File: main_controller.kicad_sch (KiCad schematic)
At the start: 1 part, among them U2 RP2040

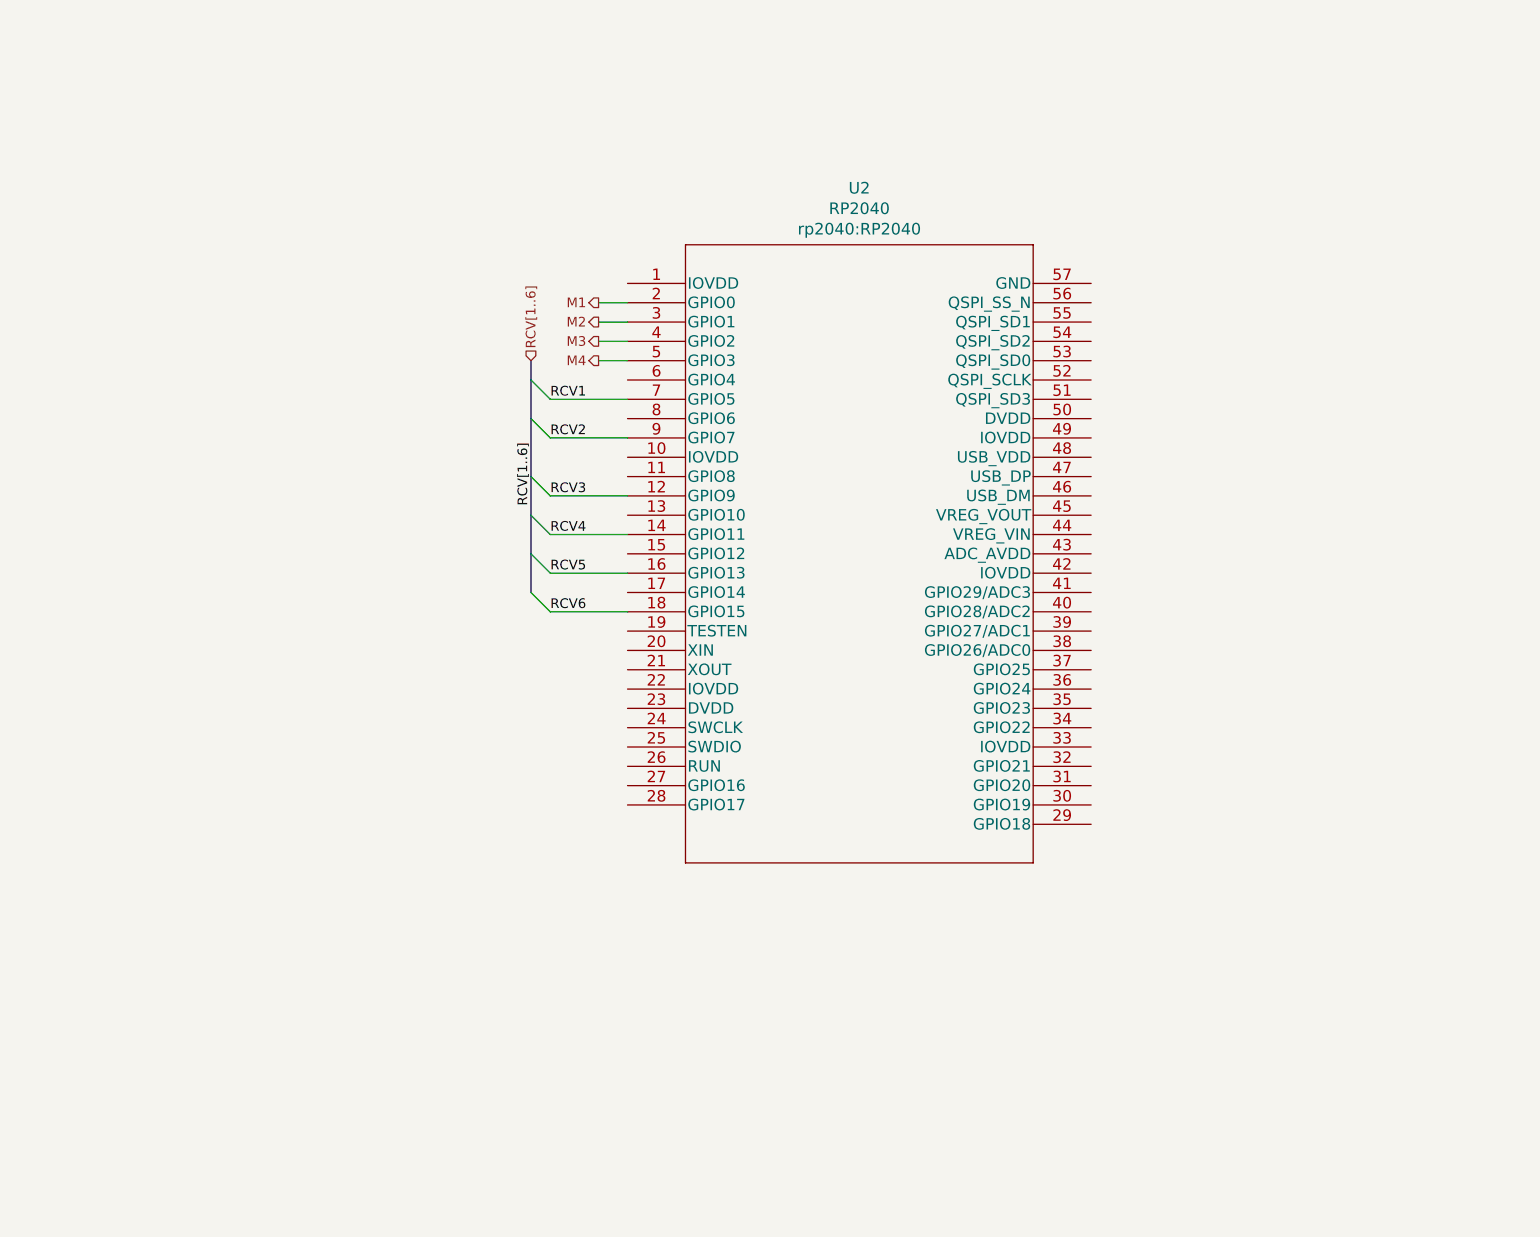
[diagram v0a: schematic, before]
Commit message: Initial schematic version
This is now a clean and ready version of the schematic:
That means:
- Schematic has been reviewed,
- It's fully annotated,
- All elements have been checked for availability with JLCPCB,
- Footprints were assigned,
- ERC is green.

No design changes should be added for this version until
the PCB is present and version is released.
Only bugfixes are possible now.
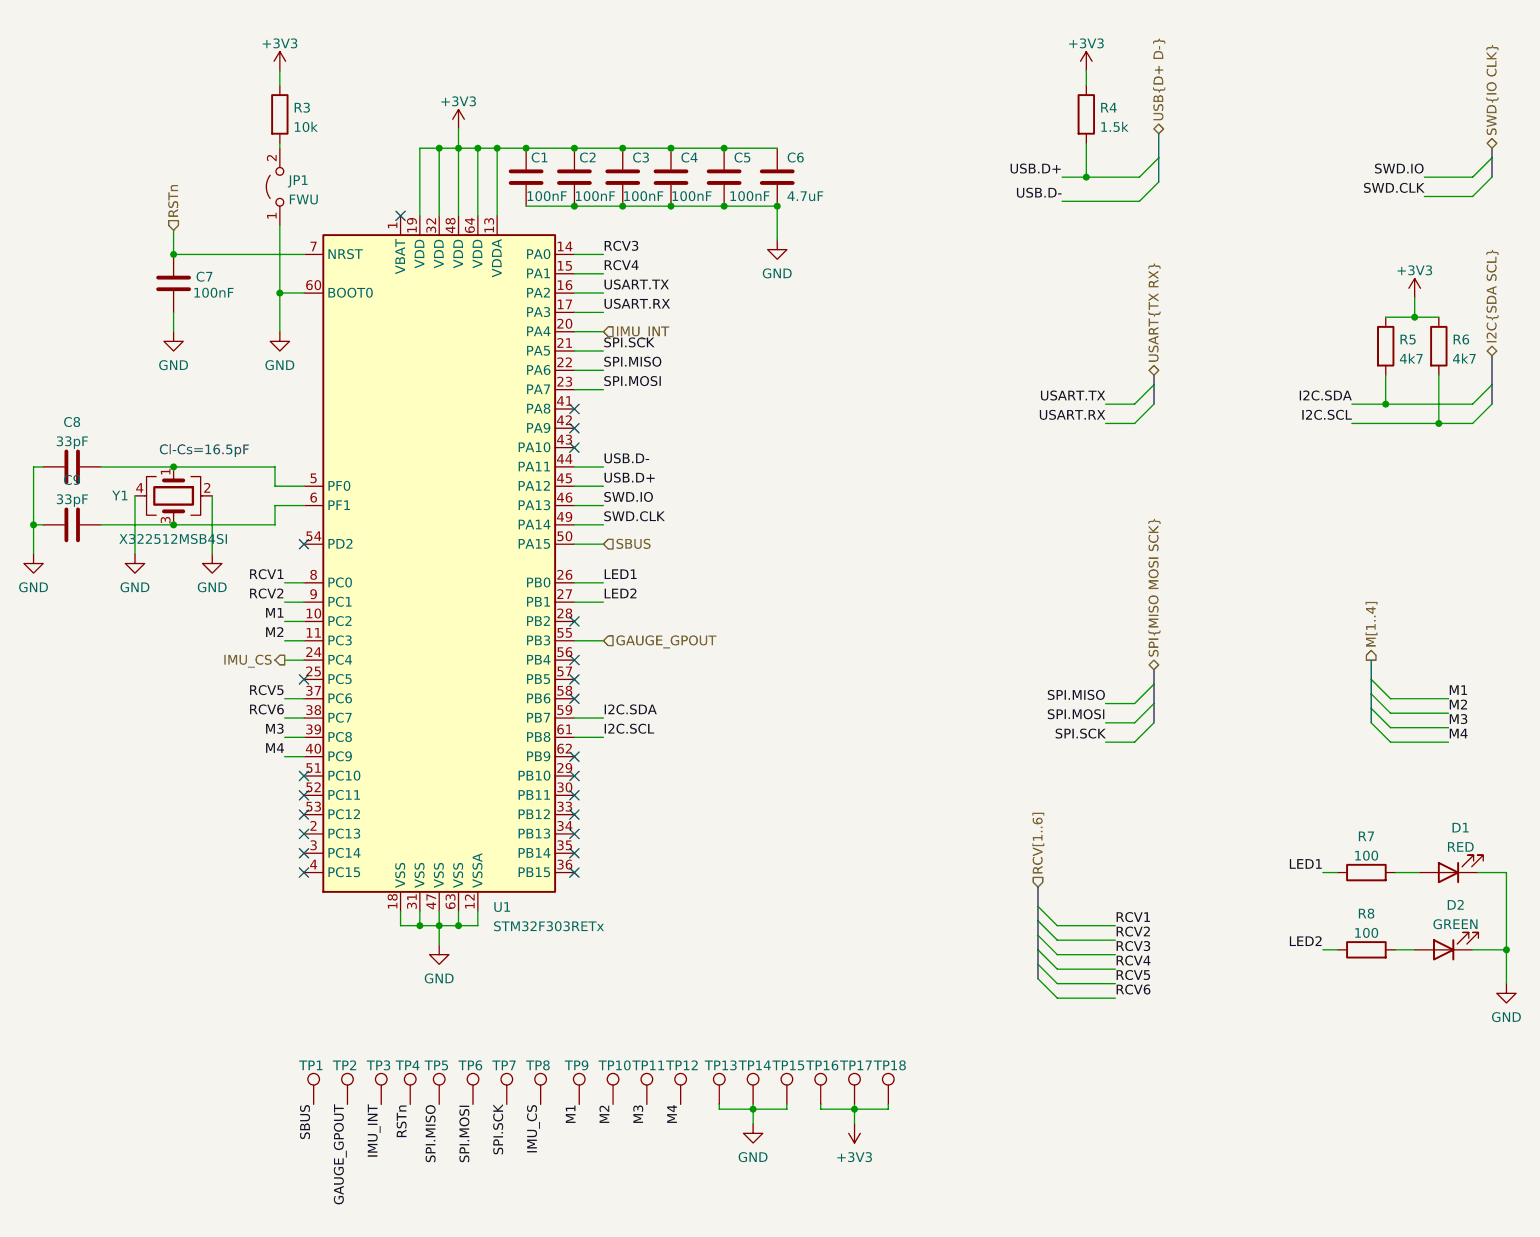
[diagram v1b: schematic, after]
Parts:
- removed U2: RP2040, rp2040:RP2040, symbol flight_controller_v2-rescue:RP2040-rp2040
- added C1, C2, C3, C4, C5, C7: 100nF, Capacitor_SMD:C_0402_1005Metric, symbol Device:C
- added C6: 4.7uF, Capacitor_SMD:C_0603_1608Metric, symbol Device:C
- added C8, C9: 33pF, Capacitor_SMD:C_0402_1005Metric, symbol Device:C
- added D1: RED, LED_SMD:LED_0402_1005Metric, symbol Device:LED
- added D2: GREEN, LED_SMD:LED_0402_1005Metric, symbol Device:LED
- added JP1: FWU, Connector_PinHeader_2.54mm:PinHeader_1x02_P2.54mm_Vertical, symbol Jumper:Jumper_2_Open
- added R3: 10k, Resistor_SMD:R_0402_1005Metric, symbol Device:R
- added R4: 1.5k, Resistor_SMD:R_0402_1005Metric, symbol Device:R
- added R5, R6: 4k7, Resistor_SMD:R_0402_1005Metric, symbol Device:R
- added R7, R8: 100, Resistor_SMD:R_0402_1005Metric, symbol Device:R
- added TP1, TP10, TP11, TP12, TP13, TP14, TP15, TP16, TP17, TP18, TP2, TP3, TP4, TP5, TP6, TP7, TP8, TP9: TestPoint, TestPoint:TestPoint_Pad_D1.0mm, symbol Connector:TestPoint
- added U1: STM32F303RETx, Package_QFP:LQFP-64_10x10mm_P0.5mm, symbol MCU_ST_STM32F3:STM32F303RETx
- added Y1: X322512MSB4SI, Crystal:Crystal_SMD_3225-4Pin_3.2x2.5mm, symbol Device:Crystal_GND24
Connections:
- net M1: now also TP9.1, U1.10 (PC2)
- net M2: now also TP10.1, U1.11 (PC3)
- net M3: now also TP11.1, U1.39 (PC8)
- net M4: now also TP12.1, U1.40 (PC9)
- net RCV1: now also U1.8 (PC0)
- net RCV2: now also U1.9 (PC1)
- net RCV3: now also U1.14 (PA0)
- net RCV4: now also U1.15 (PA1)
- net RCV5: now also U1.37 (PC6)
- net RCV6: now also U1.38 (PC7)
- new net: C8.2, U1.5 (PF0), Y1.1
- new net: C9.2, U1.6 (PF1), Y1.3
- new net: JP1.2 (B), R3.2
- new net: D1.2 (A), R7.2
- new net: D2.2 (A), R8.2
- new net +3V3: C1.1, C2.1, C3.1, C4.1, C5.1, C6.1, R3.1, R4.1, R5.1, R6.1, TP16.1, TP17.1, TP18.1, U1.13 (VDDA), U1.19 (VDD), U1.32 (VDD), U1.48 (VDD), U1.64 (VDD)
- new net GAUGE_GPOUT: TP2.1, U1.55 (PB3)
- new net GND: C1.2, C2.2, C3.2, C4.2, C5.2, C6.2, C7.2, C8.1, C9.1, D1.1 (K), D2.1 (K), JP1.1 (A), TP13.1, TP14.1, TP15.1, U1.12 (VSSA), U1.18 (VSS), U1.31 (VSS), U1.47 (VSS), U1.60 (BOOT0), U1.63 (VSS), Y1.2, Y1.4
- new net I2C.SCL: R6.2, U1.61 (PB8)
- new net I2C.SDA: R5.2, U1.59 (PB7)
- new net IMU_CS: TP8.1, U1.24 (PC4)
- new net IMU_INT: TP3.1, U1.20 (PA4)
- new net LED1: R7.1, U1.26 (PB0)
- new net LED2: R8.1, U1.27 (PB1)
- new net RSTn: C7.1, TP4.1, U1.7 (NRST)
- new net SBUS: TP1.1, U1.50 (PA15)
- new net SPI.MISO: TP5.1, U1.22 (PA6)
- new net SPI.MOSI: TP6.1, U1.23 (PA7)
- new net SPI.SCK: TP7.1, U1.21 (PA5)
- new net SWD.CLK: U1.49 (PA14)
- new net SWD.IO: U1.46 (PA13)
- new net USART.RX: U1.17 (PA3)
- new net USART.TX: U1.16 (PA2)
- new net USB.D+: R4.2, U1.45 (PA12)
- new net USB.D-: U1.44 (PA11)
- no-connect marks 0 -> 23
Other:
- note added: "Cl-Cs=16.5pF"

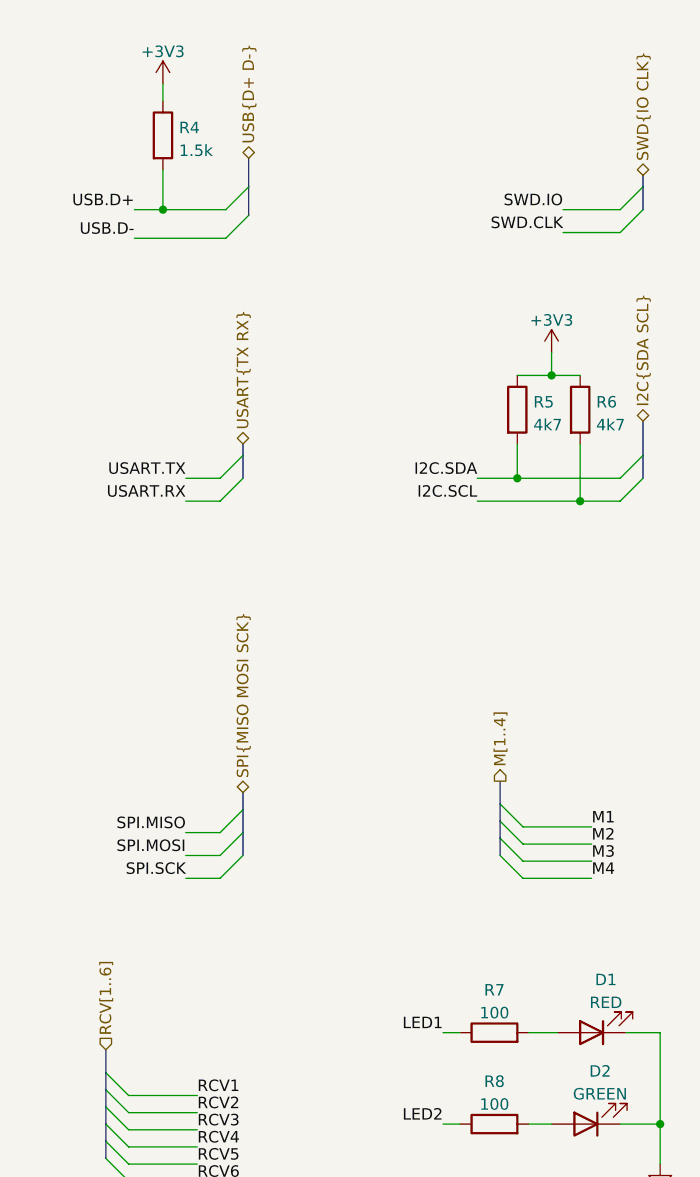
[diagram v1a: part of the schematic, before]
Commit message: Update footprints and add JLCPCB fields
Update some footprints which will suit better building the pcb
with JLCBPCB. Add fields to components sourced from JLCPCB
to be able to generate BOM.
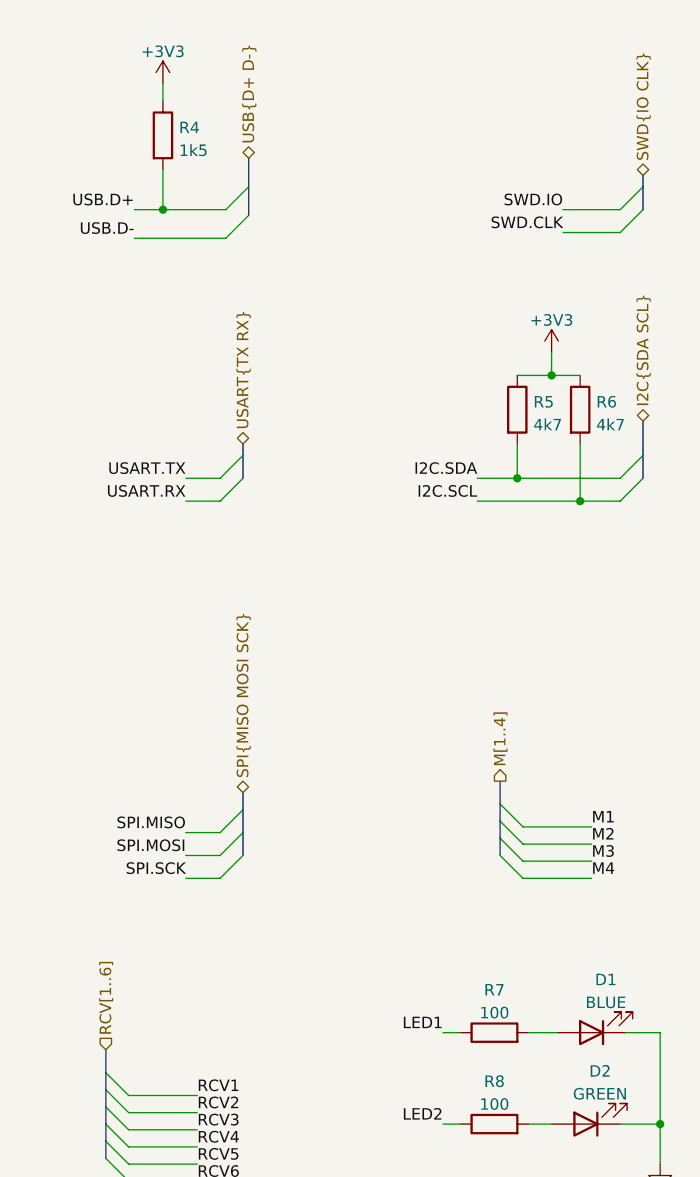
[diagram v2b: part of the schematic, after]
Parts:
- C1, C2, C3, C4, C5, C7: JLC (none) -> 0402; LCSC (none) -> C1525
- C6: footprint Capacitor_SMD:C_0603_1608Metric -> Capacitor_SMD:C_0402_1005Metric; JLC (none) -> 0402; LCSC (none) -> C23733
- C8, C9: JLC (none) -> 0402; LCSC (none) -> C1562
- D1: value RED -> BLUE; footprint LED_SMD:LED_0402_1005Metric -> LED_SMD:LED_0603_1608Metric; JLC (none) -> 0603; LCSC (none) -> C72041
- D2: footprint LED_SMD:LED_0402_1005Metric -> LED_SMD:LED_0603_1608Metric; JLC (none) -> 0603; LCSC (none) -> C72043
- R3: JLC (none) -> 0402; LCSC (none) -> C25744
- R4: value 1.5k -> 1k5; JLC (none) -> 0402; LCSC (none) -> C25867
- R5, R6: JLC (none) -> 0402; LCSC (none) -> C25900
- R7, R8: JLC (none) -> 0402; LCSC (none) -> C25076
- U1: JLC (none) -> LQFP-64(10x10); LCSC (none) -> C183214
- Y1: JLC (none) -> SMD3225-4P; LCSC (none) -> C9002
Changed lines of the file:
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@@
+      (effects (font (size 1.27 1.27)) hide)
+    )
+    (property "JLC" "LQFP-64(10x10)" (id 4) (at 89.535 96.52 0)
+      (effects (font (size 1.27 1.27)) hide)
+    )
+    (property "LCSC" "C183214" (id 5) (at 89.535 96.52 0)
       (effects (font (size 1.27 1.27)) hide)
     )
@@
       (effects (font (size 1.27 1.27)) (justify left))
     )
-    (property "Value" "1.5k" (id 1) (at 176.403 39.1672 0)
+    (property "Value" "1k5" (id 1) (at 176.403 39.1672 0)
       (effects (font (size 1.27 1.27)) (justify left))
     )
@@
     )
     (property "Datasheet" "~" (id 3) (at 174.625 37.465 0)
+      (effects (font (size 1.27 1.27)) hide)
+    )
+    (property "JLC" "0402" (id 4) (at 174.625 37.465 0)
+      (effects (font (size 1.27 1.27)) hide)
+    )
+    (property "LCSC" " C25867" (id 5) (at 174.625 37.465 0)
       (effects (font (size 1.27 1.27)) hide)
     )
@@
     )
     (property "Datasheet" "~" (id 3) (at 213.995 67.945 0)
+      (effects (font (size 1.27 1.27)) hide)
+    )
+    (property "JLC" "0402" (id 4) (at 213.995 67.945 0)
+      (effects (font (size 1.27 1.27)) hide)
+    )
+    (property "LCSC" " C25900" (id 5) (at 213.995 67.945 0)
       (effects (font (size 1.27 1.27)) hide)
     )
@@
       (effects (font (size 1.27 1.27)) hide)
     )
+    (property "JLC" "0402" (id 4) (at 211.455 137.16 0)
+      (effects (font (size 1.27 1.27)) hide)
+    )
+    (property "LCSC" " C25076" (id 5) (at 211.455 137.16 0)
+      (effects (font (size 1.27 1.27)) hide)
+    )
     (pin "1")
     (pin "2")
@@
     )
     (property "Datasheet" "~" (id 3) (at 68.58 37.465 0)
+      (effects (font (size 1.27 1.27)) hide)
+    )
+    (property "JLC" "0402" (id 4) (at 68.58 37.465 0)
+      (effects (font (size 1.27 1.27)) hide)
+    )
+    (property "LCSC" " C25744" (id 5) (at 68.58 37.465 0)
       (effects (font (size 1.27 1.27)) hide)
     )
@@
       (effects (font (size 1.27 1.27)) hide)
     )
+    (property "JLC" "0402" (id 4) (at 41.275 83.82 0)
+      (effects (font (size 1.27 1.27)) hide)
+    )
+    (property "LCSC" "C1562" (id 5) (at 41.275 83.82 0)
+      (effects (font (size 1.27 1.27)) hide)
+    )
     (pin "1")
     (pin "2")
@@
       (effects (font (size 1.27 1.27)) hide)
     )
+    (property "JLC" "0402" (id 4) (at 127 45.72 0)
+      (effects (font (size 1.27 1.27)) hide)
+    )
+    (property "LCSC" "C1525" (id 5) (at 127 45.72 0)
+      (effects (font (size 1.27 1.27)) hide)
+    )
     (pin "1")
     (pin "2")
@@
       (effects (font (size 1.27 1.27)) hide)
     )
+    (property "JLC" "0402" (id 4) (at 120.015 45.72 0)
+      (effects (font (size 1.27 1.27)) hide)
+    )
+    (property "LCSC" "C1525" (id 5) (at 120.015 45.72 0)
+      (effects (font (size 1.27 1.27)) hide)
+    )
     (pin "1")
     (pin "2")
@@
     )
     (property "Datasheet" "~" (id 3) (at 100.965 45.72 0)
+      (effects (font (size 1.27 1.27)) hide)
+    )
+    (property "JLC" "0402" (id 4) (at 100.965 45.72 0)
+      (effects (font (size 1.27 1.27)) hide)
+    )
+    (property "LCSC" "C1525" (id 5) (at 100.965 45.72 0)
       (effects (font (size 1.27 1.27)) hide)
     )
@@
       (effects (font (size 1.27 1.27)) hide)
     )
+    (property "JLC" "0402" (id 4) (at 211.455 147.32 0)
+      (effects (font (size 1.27 1.27)) hide)
+    )
+    (property "LCSC" " C25076" (id 5) (at 211.455 147.32 0)
+      (effects (font (size 1.27 1.27)) hide)
+    )
     (pin "1")
     (pin "2")
@@
     (in_bom yes) (on_board yes) (fields_autoplaced)
     (property "Reference" "D1" (id 0) (at 223.8375 131.3012 0))
-    (property "Value" "RED" (id 1) (at 223.8375 133.8381 0))
-    (property "Footprint" "LED_SMD:LED_0402_1005Metric" (id 2) (at 222.25 137.16 0)
+    (property "Value" "BLUE" (id 1) (at 223.8375 133.8381 0))
+    (property "Footprint" "LED_SMD:LED_0603_1608Metric" (id 2) (at 222.25 137.16 0)
       (effects (font (size 1.27 1.27)) hide)
     )
     (property "Datasheet" "~" (id 3) (at 222.25 137.16 0)
+      (effects (font (size 1.27 1.27)) hide)
+    )
+    (property "JLC" "0603" (id 4) (at 222.25 137.16 0)
+      (effects (font (size 1.27 1.27)) hide)
+    )
+    (property "LCSC" "C72041" (id 5) (at 222.25 137.16 0)
       (effects (font (size 1.27 1.27)) hide)
     )
@@
     (property "Reference" "D2" (id 0) (at 223.2025 141.4612 0))
     (property "Value" "GREEN" (id 1) (at 223.2025 143.9981 0))
-    (property "Footprint" "LED_SMD:LED_0402_1005Metric" (id 2) (at 221.615 147.32 0)
+    (property "Footprint" "LED_SMD:LED_0603_1608Metric" (id 2) (at 221.615 147.32 0)
       (effects (font (size 1.27 1.27)) hide)
     )
     (property "Datasheet" "~" (id 3) (at 221.615 147.32 0)
+      (effects (font (size 1.27 1.27)) hide)
+    )
+    (property "JLC" "0603" (id 4) (at 221.615 147.32 0)
+      (effects (font (size 1.27 1.27)) hide)
+    )
+    (property "LCSC" "C72043" (id 5) (at 221.615 147.32 0)
       (effects (font (size 1.27 1.27)) hide)
     )
@@
       (effects (font (size 1.27 1.27)) hide)
     )
+    (property "JLC" "0402" (id 4) (at 54.61 59.69 0)
+      (effects (font (size 1.27 1.27)) hide)
+    )
+    (property "LCSC" "C1525" (id 5) (at 54.61 59.69 0)
+      (effects (font (size 1.27 1.27)) hide)
+    )
     (pin "1")
     (pin "2")
@@
       (effects (font (size 1.27 1.27)) hide)
     )
+    (property "JLC" "0402" (id 4) (at 113.665 45.72 0)
+      (effects (font (size 1.27 1.27)) hide)
+    )
+    (property "LCSC" "C1525" (id 5) (at 113.665 45.72 0)
+      (effects (font (size 1.27 1.27)) hide)
+    )
     (pin "1")
     (pin "2")
@@
       (effects (font (size 1.27 1.27)) (justify left))
     )
-    (property "Footprint" "Capacitor_SMD:C_0603_1608Metric" (id 2) (at 134.9502 49.53 0)
+    (property "Footprint" "Capacitor_SMD:C_0402_1005Metric" (id 2) (at 134.9502 49.53 0)
       (effects (font (size 1.27 1.27)) hide)
     )
@@
       (effects (font (size 1.27 1.27)) hide)
     )
+    (property "JLC" "0402" (id 4) (at 133.985 45.72 0)
+      (effects (font (size 1.27 1.27)) hide)
+    )
+    (property "LCSC" "C23733" (id 5) (at 133.985 45.72 0)
+      (effects (font (size 1.27 1.27)) hide)
+    )
     (pin "1")
     (pin "2")
@@
     )
     (property "Datasheet" "~" (id 3) (at 107.315 45.72 0)
+      (effects (font (size 1.27 1.27)) hide)
+    )
+    (property "JLC" "0402" (id 4) (at 107.315 45.72 0)
+      (effects (font (size 1.27 1.27)) hide)
+    )
+    (property "LCSC" "C1525" (id 5) (at 107.315 45.72 0)
       (effects (font (size 1.27 1.27)) hide)
     )
@@
       (effects (font (size 1.27 1.27)) hide)
     )
+    (property "JLC" "SMD3225-4P" (id 4) (at 54.61 87.63 0)
+      (effects (font (size 1.27 1.27)) hide)
+    )
+    (property "LCSC" "C9002" (id 5) (at 54.61 87.63 0)
+      (effects (font (size 1.27 1.27)) hide)
+    )
     (pin "1")
     (pin "2")
@@
       (effects (font (size 1.27 1.27)) hide)
     )
+    (property "JLC" "0402" (id 4) (at 41.275 91.44 0)
+      (effects (font (size 1.27 1.27)) hide)
+    )
+    (property "LCSC" "C1562" (id 5) (at 41.275 91.44 0)
+      (effects (font (size 1.27 1.27)) hide)
+    )
     (pin "1")
     (pin "2")
@@
       (effects (font (size 1.27 1.27)) hide)
     )
+    (property "JLC" "0402" (id 4) (at 220.98 67.945 0)
+      (effects (font (size 1.27 1.27)) hide)
+    )
+    (property "LCSC" " C25900" (id 5) (at 220.98 67.945 0)
+      (effects (font (size 1.27 1.27)) hide)
+    )
